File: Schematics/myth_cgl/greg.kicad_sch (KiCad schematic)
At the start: 6 parts, among them U15 74HC193, U16 74HC193, U17 74AHC244, U18 74AHC574, U5 74LS08, U7 74HC02

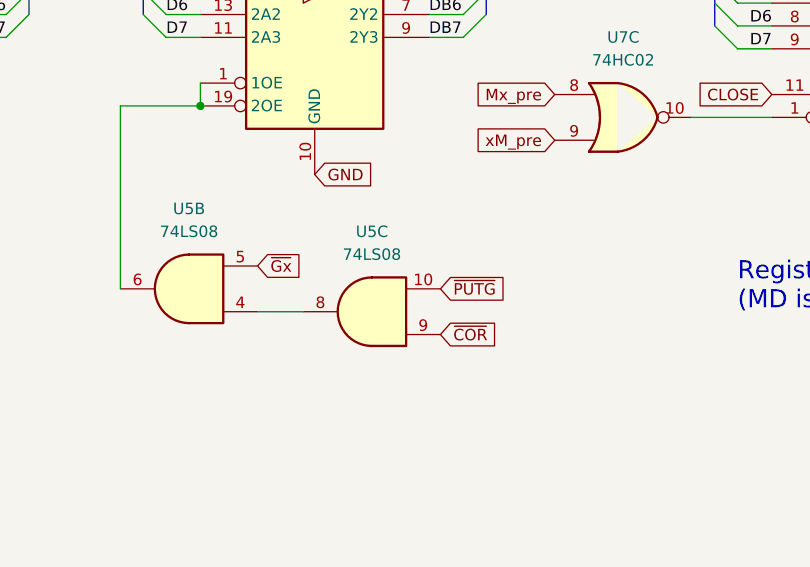
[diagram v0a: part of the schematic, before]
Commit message: Change COR to use R
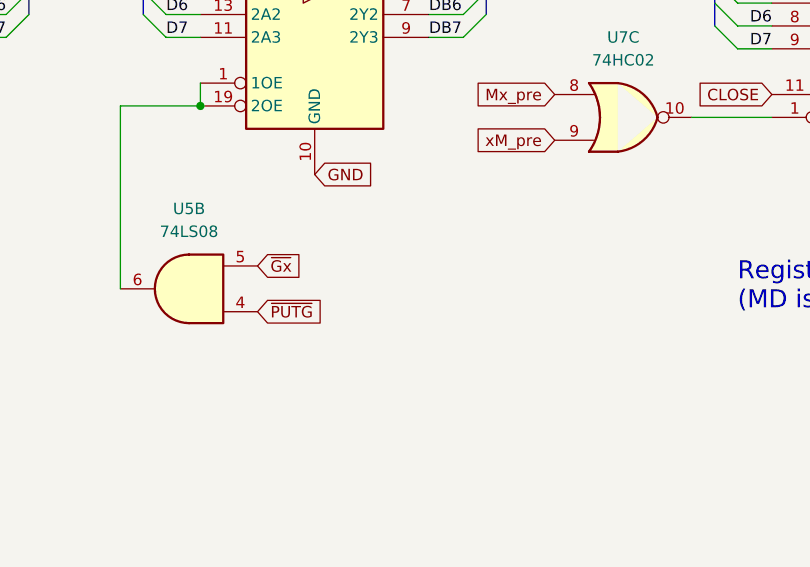
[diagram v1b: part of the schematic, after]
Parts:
- removed unit 3 of U5
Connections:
- net ~{PUTG}: now also U5.4
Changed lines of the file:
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@@
-	(wire
-		(pts
-			(xy 161.29 107.95) (xy 166.37 107.95)
-		)
-		(stroke
-			(width 0)
-			(type default)
-		)
-	)
 	(wire
 		(pts
@@
 	(global_label "~{PUTG}"
 		(shape input)
-		(at 181.61 105.41 0)
+		(at 161.29 107.95 0)
 		(fields_autoplaced yes)
 		(effects
@@
 		)
 		(property "Intersheetrefs" "${INTERSHEET_REFS}"
-			(at 189.4333 105.41 0)
+			(at 169.1133 107.95 0)
 			(effects
 				(font
@@
 				)
 				(justify right)
-				(hide yes)
-			)
-		)
-	)
-	(global_label "~{COR}"
-		(shape input)
-		(at 181.61 110.49 0)
-		(fields_autoplaced yes)
-		(effects
-			(font
-				(size 1.27 1.27)
-			)
-			(justify left)
-		)
-		(property "Intersheetrefs" "${INTERSHEET_REFS}"
-			(at 188.4657 110.49 0)
-			(effects
-				(font
-					(size 1.27 1.27)
-				)
-				(justify left)
 				(hide yes)
 			)
@@
 					(unit 3)
 				)
-			)
-		)
-	)
-	(symbol
-		(lib_id "74xx:74LS08")
-		(at 173.99 107.95 180)
-		(unit 3)
-		(exclude_from_sim no)
-		(in_bom yes)
-		(on_board yes)
-		(dnp no)
-		(fields_autoplaced yes)
-		(property "Reference" "U5"
-			(at 173.9983 99.06 0)
-			(effects
-				(font
-					(size 1.27 1.27)
-				)
-			)
-		)
-		(property "Value" "74LS08"
-			(at 173.9983 101.6 0)
-			(effects
-				(font
-					(size 1.27 1.27)
-				)
-			)
-		)
-		(property "Footprint" "Package_DIP:DIP-14_W7.62mm_LongPads"
-			(at 173.99 107.95 0)
-			(effects
-				(font
-					(size 1.27 1.27)
-				)
-				(hide yes)
-			)
-		)
-		(property "Datasheet" "http://www.ti.com/lit/gpn/sn74LS08"
-			(at 173.99 107.95 0)
-			(effects
-				(font
-					(size 1.27 1.27)
-				)
-				(hide yes)
-			)
-		)
-		(property "Description" "Quad And2"
-			(at 173.99 107.95 0)
-			(effects
-				(font
-					(size 1.27 1.27)
-				)
-				(hide yes)
-			)
-		)
-		(pin "2"
-		)
-		(pin "11"
-		)
-		(pin "4"
-		)
-		(pin "12"
-		)
-		(pin "13"
-		)
-		(pin "1"
-		)
-		(pin "3"
-		)
-		(pin "8"
-		)
-		(pin "9"
-		)
-		(pin "5"
-		)
-		(pin "10"
-		)
-		(pin "6"
-		)
-		(pin "14"
-		)
-		(pin "7"
-		)
-		(instances
-			(project "myth_cgl"
-				(path "/fc80d15a-8391-4108-8bee-dfbcee45d6bc/99537f26-a95b-4a0f-9442-409c0e5998d5"
-					(reference "U5")
-					(unit 3)
-				)

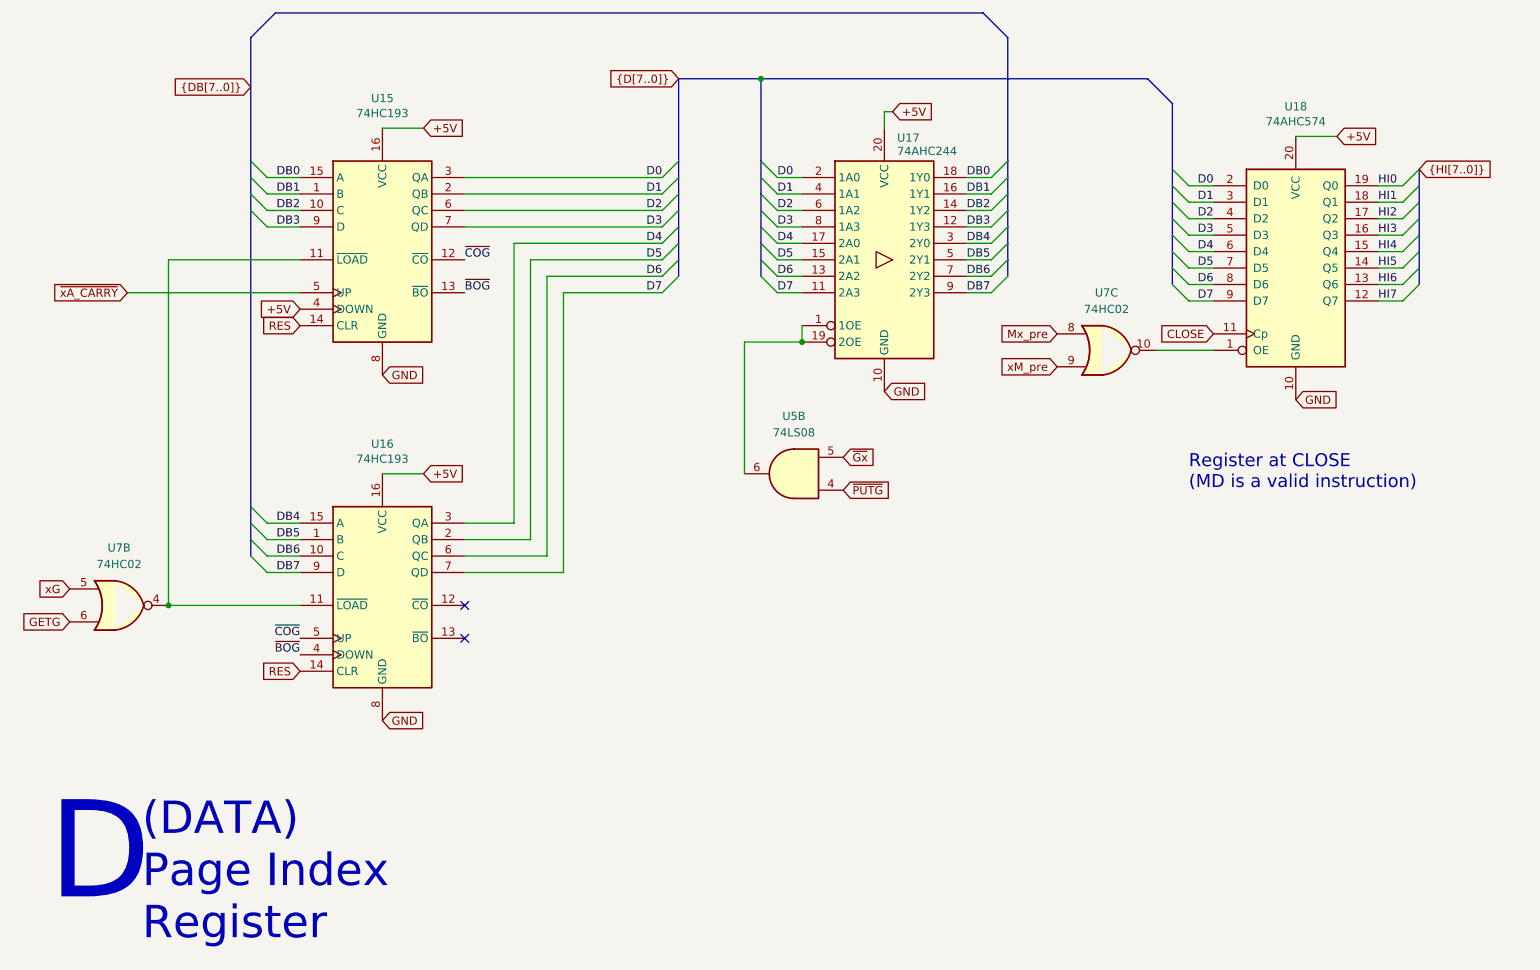
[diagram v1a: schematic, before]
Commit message: Change semantics of xB
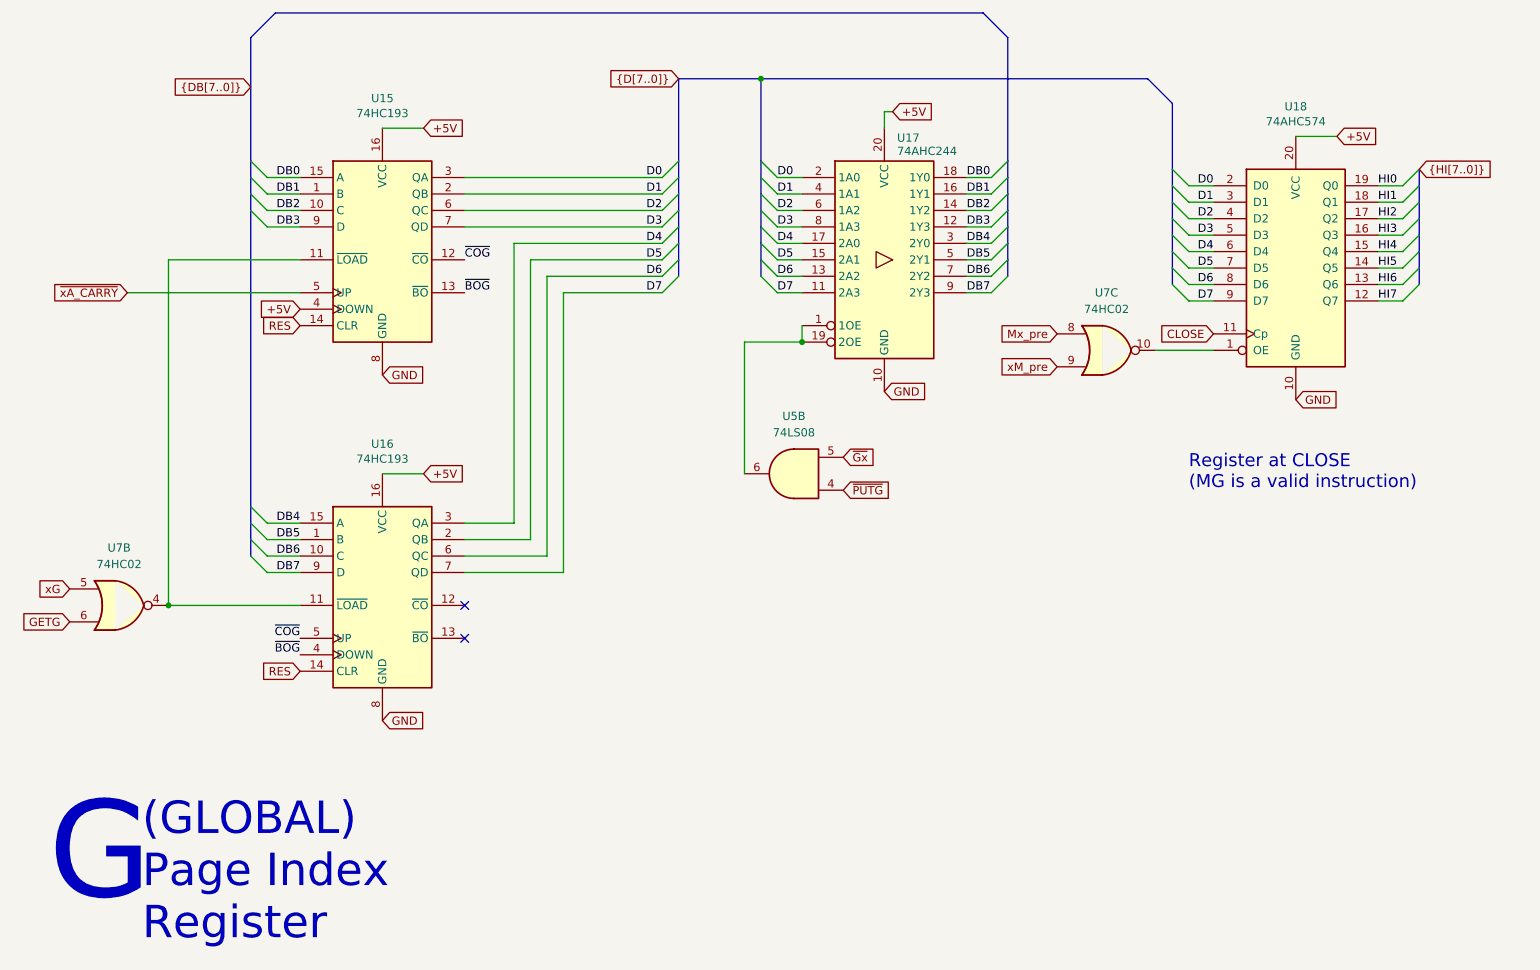
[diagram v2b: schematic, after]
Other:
- note added: "(GLOBAL) Page Index Register"
- note added: "G"
- note added: "Register at CLOSE (MG is a valid instruction)"
- note removed: "(DATA) Page Index Register"
- note removed: "D"
- note removed: "Register at CLOSE (MD is a valid instruction)"
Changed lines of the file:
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@@
 		)
 	)
-	(text "(DATA)\nPage Index\nRegister"
+	(text "(GLOBAL)\nPage Index\nRegister"
 		(exclude_from_sim no)
 		(at 53.086 177.8 0)
@@
 		)
 	)
-	(text "Register at CLOSE\n(MD is a valid instruction)"
+	(text "Register at CLOSE\n(MG is a valid instruction)"
 		(exclude_from_sim no)
 		(at 214.63 107.95 0)
@@
 		)
 	)
-	(text "D"
+	(text "G"
 		(exclude_from_sim no)
 		(at 38.608 172.72 0)
